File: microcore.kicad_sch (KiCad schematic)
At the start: 5 parts, among them J1 TE_776231-1, J8 USB_B_Mini, M1 Module:mega-mcu100/0.3, M2 Module-power_12and5V-0.3, M3 Module-vr-max9924-0.3

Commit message: Rev p: AOD4184A (C99124) + LS US1M/SMAJ33A + DRC (#9)
* Rev p: AOD4184A on Q1-Q7, LS flyback+TVS, frame short fixes

Quintin chose AOD4184A (LCSC C99124) plus TVS for budget and reliability.
Q5-Q7 get the existing US1M flyback and SMAJ33A. Injector/VR frame shorts
on the board copper are cleared; Hellen module pad-G noise stays documented.

Co-authored-by: Quintin <quintinbannink42@users.noreply.github.com>

* Rev p: keep Q1-Q7 as NCE4080K; LS US1M+SMAJ33A stays

Budget and reliability first. No FET or BOM upgrade and no DPAK land change. Low-side clamps stay the injector US1M and SMAJ33A already in the BOM.

Co-authored-by: Quintin <quintinbannink42@users.noreply.github.com>

---------

Co-authored-by: Quintin <quintinbannink42@users.noreply.github.com>
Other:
- sheet LS3 ports: added V12_RAW; removed none
- note added: "AMPSEAL pins 8/9/10: FP / Idle / Boost (rev p) Q5-Q7 AOD4184A + gate R5-R7 12 ohm + US1M flyback + SMAJ33A"
- note added: "Micro Core rev P MCU mega-mcu100/0.3 STM32F407VGT6 (not mega-mcu64) + power_12and5V/0.3 + vr-max9924/0.3 USB Mini-B + TE 776231-1 AMPSEAL; pins 8/9/10 FP / Idle / Boost Sheets: INJ4 (Q1-Q4) LS3 (Q5-Q7) ANALOG HALL Power FETs AOD4184A C99124. RDS(on) at 4.5 V; Vth max 2.6 V; gate is 3.3 V. coreefi_micro needs F407 target later"
- note removed: "AMPSEAL pins 8/9/10: FP / Idle / Boost (rev o) Q5-Q7 NCE4080K + gate R5-R7 12 ohm"
- note removed: "Micro Core rev O MCU mega-mcu100/0.3 STM32F407VGT6 (not mega-mcu64) + power_12and5V/0.3 + vr-max9924/0.3 USB Mini-B + TE 776231-1 AMPSEAL; pins 8/9/10 FP / Idle / Boost Sheets: INJ4 (Q1-Q4) LS3 (Q5-Q7) ANALOG HALL Power FETs NCE4080K C191380. coreefi_micro needs F407 target later"
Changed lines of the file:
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@@
 	(title_block
 		(title "Micro Core")
-		(date "2026-09-22")
-		(rev "O")
+		(date "2026-09-24")
+		(rev "P")
 		(company "Core EFI")
-		(comment 1 "rev o: NCE4080K Q1-Q7; LS Q5-Q7 restored; F407VGT6 stays")
+		(comment 1 "rev p: AOD4184A Q1-Q7 C99124; LS flyback+TVS; F407VGT6 stays")
 		(comment 2 "Firmware board: coreefi_micro — needs F407 target later; fw not in this repo")
 		(comment 3 "PCB basename: microcore (no dashes/underscores)")
@@
 			)
 		)
+		(pin "V12_RAW" input
+			(at 17.78 70.14 90)
+			(effects
+				(font
+					(size 1.27 1.27)
+				)
+				(justify left)
+			)
+		)
 		(instances
 			(project "microcore"
@@
 		)
 	)
-	(text "Micro Core rev O\nMCU mega-mcu100/0.3 STM32F407VGT6 (not mega-mcu64) + power_12and5V/0.3 + vr-max9924/0.3\nUSB Mini-B + TE 776231-1 AMPSEAL; pins 8/9/10 FP / Idle / Boost\nSheets: INJ4 (Q1-Q4) LS3 (Q5-Q7) ANALOG HALL\nPower FETs NCE4080K C191380. coreefi_micro needs F407 target later"
+	(text "Micro Core rev P\nMCU mega-mcu100/0.3 STM32F407VGT6 (not mega-mcu64) + power_12and5V/0.3 + vr-max9924/0.3\nUSB Mini-B + TE 776231-1 AMPSEAL; pins 8/9/10 FP / Idle / Boost\nSheets: INJ4 (Q1-Q4) LS3 (Q5-Q7) ANALOG HALL\nPower FETs AOD4184A C99124. RDS(on) at 4.5 V; Vth max 2.6 V; gate is 3.3 V. coreefi_micro needs F407 target later"
 		(exclude_from_sim no)
 		(at 25.4 280 0)
@@
 		)
 	)
-	(text "AMPSEAL pins 8/9/10: FP / Idle / Boost (rev o)\nQ5-Q7 NCE4080K + gate R5-R7 12 ohm"
+	(text "AMPSEAL pins 8/9/10: FP / Idle / Boost (rev p)\nQ5-Q7 AOD4184A + gate R5-R7 12 ohm + US1M flyback + SMAJ33A"
 		(exclude_from_sim no)
 		(at 230 43.18 0)
 		(effects
 			(font
+				(size 1.27 1.27)
+			)
+			(justify left bottom)
+		)
+	)
+	(wire
+		(pts
+			(xy 17.78 70.14) (xy 17.78 67.31)
+		)
+		(stroke
+			(width 0)
+			(type default)
+		)
+	)
+	(label "V12_RAW"
+		(at 17.78 67.31 90)
+		(effects
+			(font

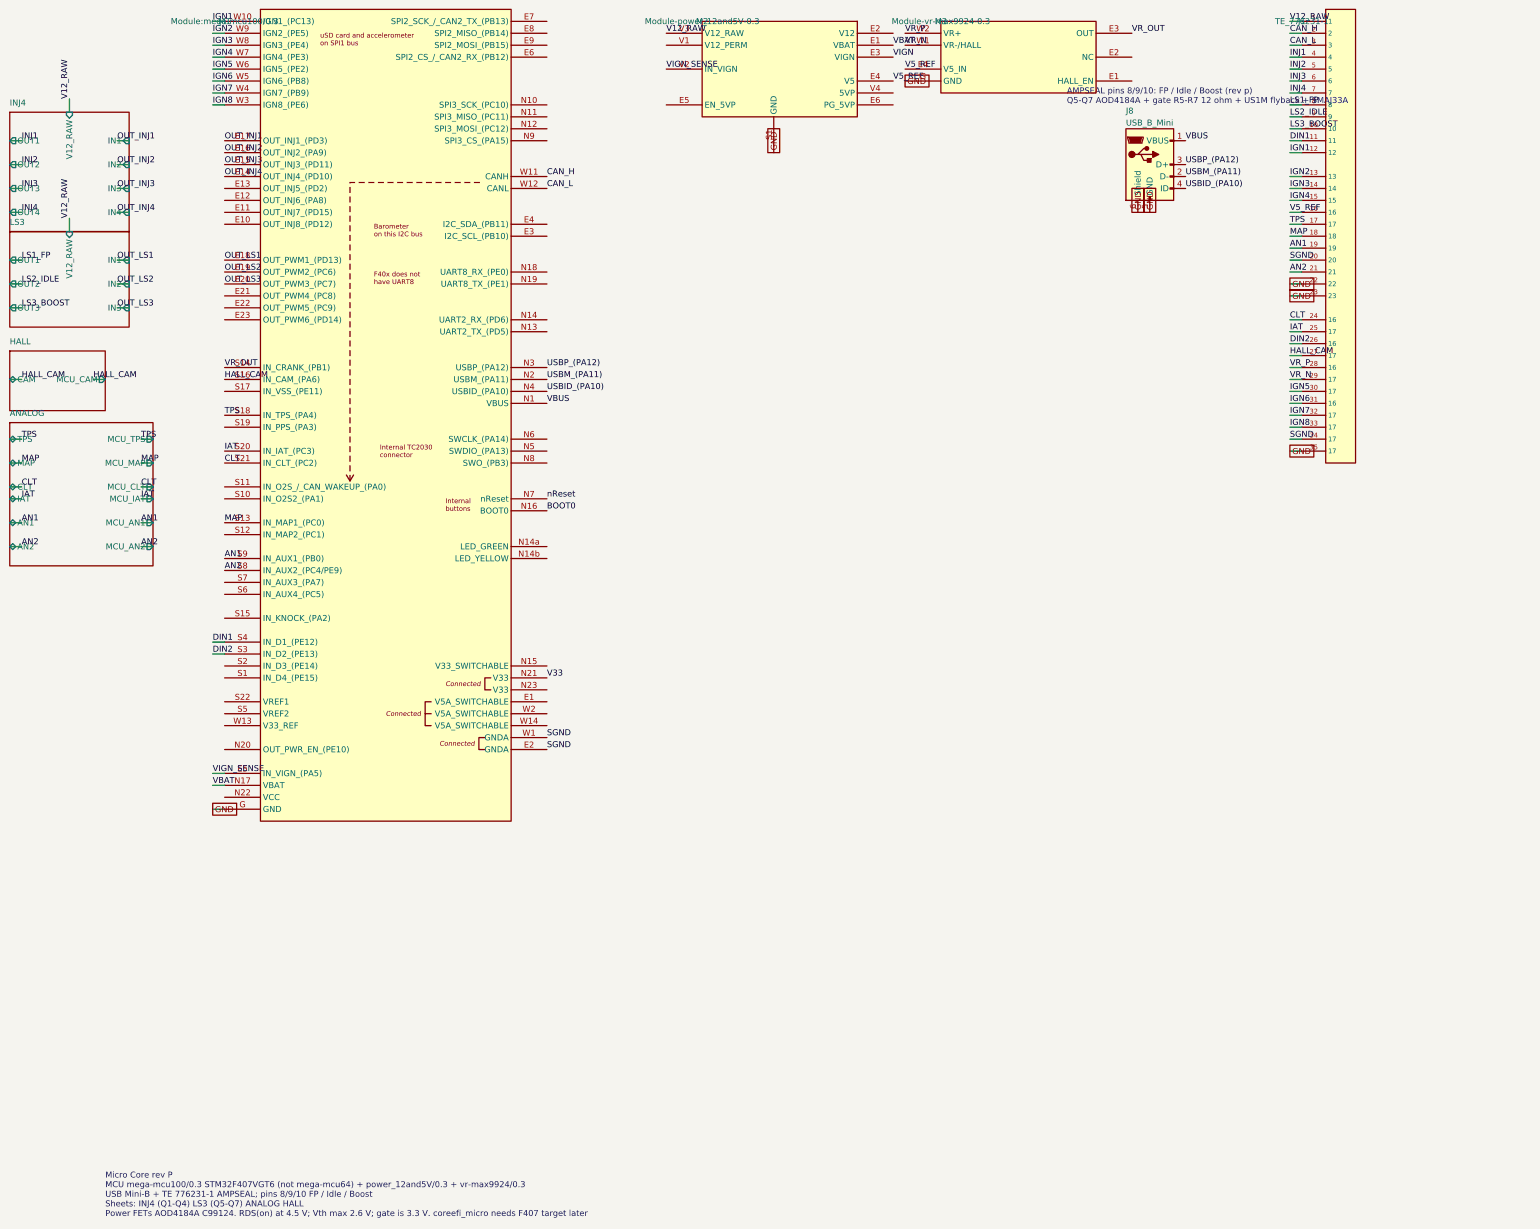
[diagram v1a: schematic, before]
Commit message: Rev q: NCE4080K (C191380) plus SLM27524 gate drivers on V12_RAW
Restore Q1-Q7 to NCE4080K and insert four SLM27524CA-DG drivers so the
STM32 GPIO no longer drives the FET gates. Seven channels are used; the
spare input is tied to GND. LS clamps and the rev p short fixes stay.

Co-authored-by: Quintin <quintinbannink42@users.noreply.github.com>
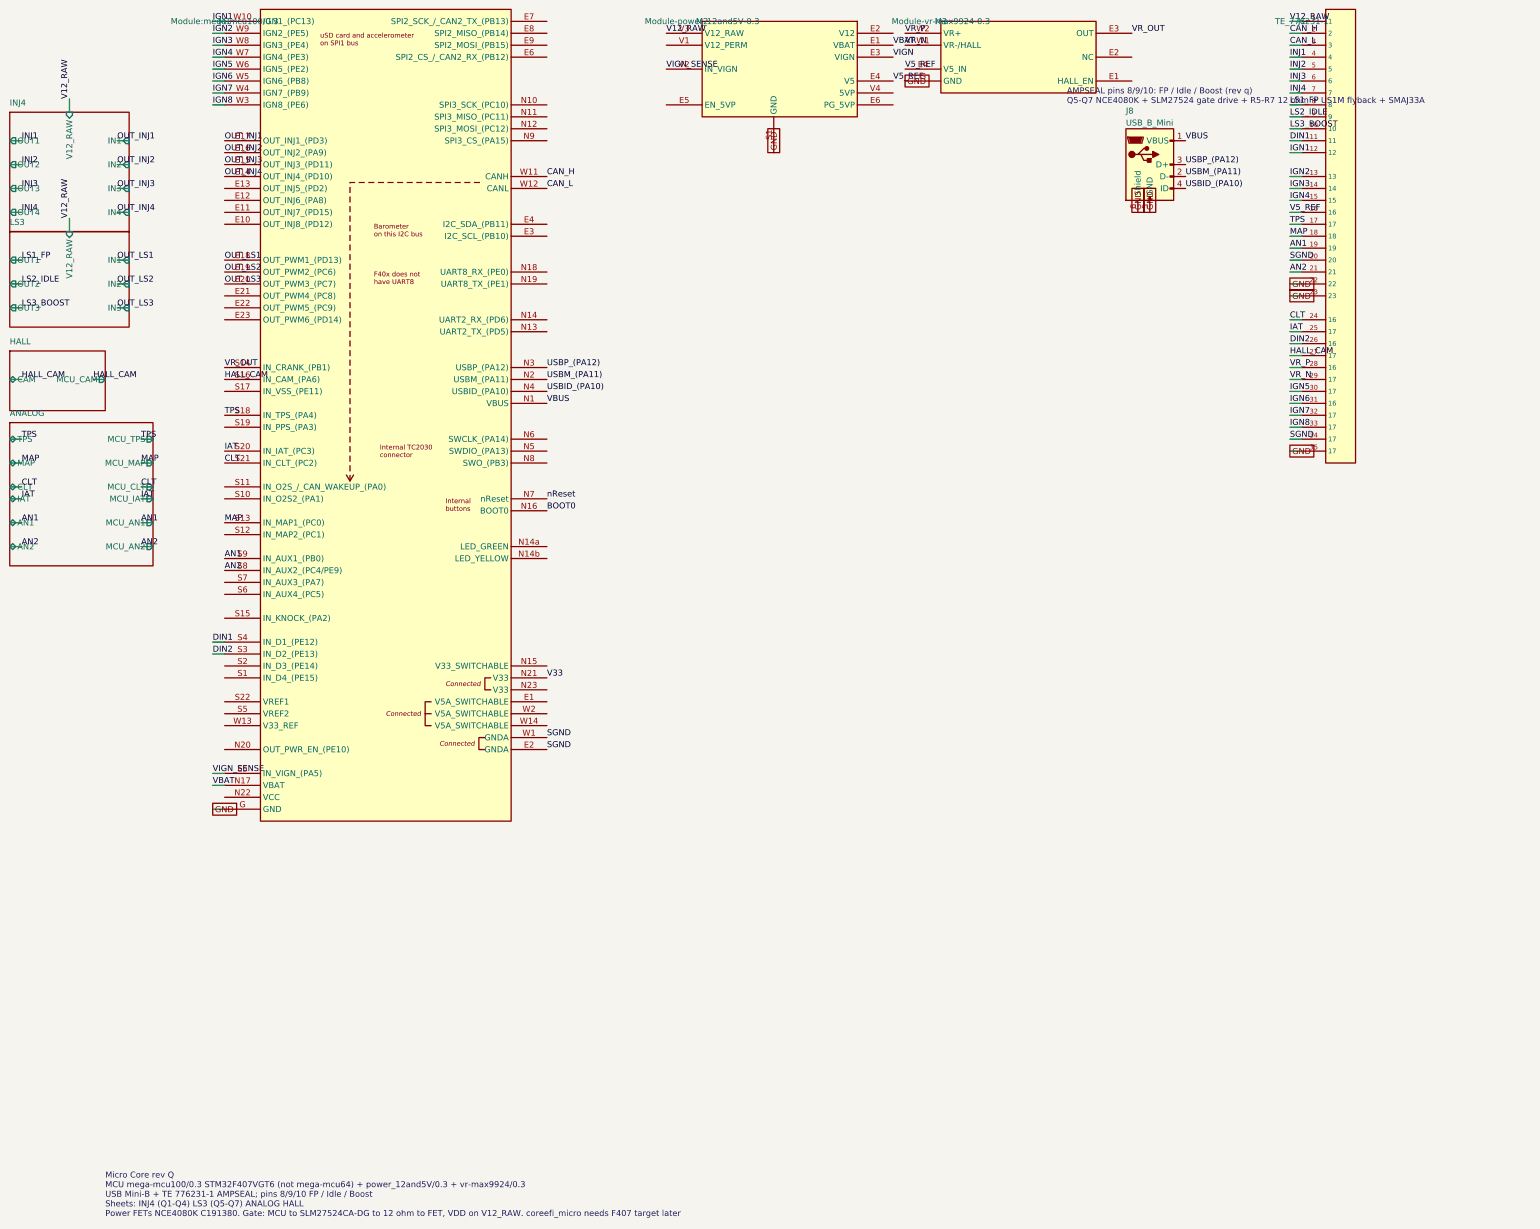
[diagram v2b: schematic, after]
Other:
- note added: "AMPSEAL pins 8/9/10: FP / Idle / Boost (rev q) Q5-Q7 NCE4080K + SLM27524 gate drive + R5-R7 12 ohm + US1M flyback + SMAJ33A"
- note added: "Micro Core rev Q MCU mega-mcu100/0.3 STM32F407VGT6 (not mega-mcu64) + power_12and5V/0.3 + vr-max9924/0.3 USB Mini-B + TE 776231-1 AMPSEAL; pins 8/9/10 FP / Idle / Boost Sheets: INJ4 (Q1-Q4) LS3 (Q5-Q7) ANALOG HALL Power FETs NCE4080K C191380. Gate: MCU to SLM27524CA-DG to 12 ohm to FET, VDD on V12_RAW. coreefi_micro needs F407 target later"
- note removed: "AMPSEAL pins 8/9/10: FP / Idle / Boost (rev p) Q5-Q7 AOD4184A + gate R5-R7 12 ohm + US1M flyback + SMAJ33A"
- note removed: "Micro Core rev P MCU mega-mcu100/0.3 STM32F407VGT6 (not mega-mcu64) + power_12and5V/0.3 + vr-max9924/0.3 USB Mini-B + TE 776231-1 AMPSEAL; pins 8/9/10 FP / Idle / Boost Sheets: INJ4 (Q1-Q4) LS3 (Q5-Q7) ANALOG HALL Power FETs AOD4184A C99124. RDS(on) at 4.5 V; Vth max 2.6 V; gate is 3.3 V. coreefi_micro needs F407 target later"
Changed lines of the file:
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@@
 	(title_block
 		(title "Micro Core")
-		(date "2026-09-24")
-		(rev "P")
+		(date "2026-09-26")
+		(rev "Q")
 		(company "Core EFI")
-		(comment 1 "rev p: AOD4184A Q1-Q7 C99124; LS flyback+TVS; F407VGT6 stays")
+		(comment 1 "rev q: NCE4080K Q1-Q7 C191380; SLM27524 gate drivers; LS clamps kept")
 		(comment 2 "Firmware board: coreefi_micro — needs F407 target later; fw not in this repo")
 		(comment 3 "PCB basename: microcore (no dashes/underscores)")
@@
 		)
 	)
-	(text "Micro Core rev P\nMCU mega-mcu100/0.3 STM32F407VGT6 (not mega-mcu64) + power_12and5V/0.3 + vr-max9924/0.3\nUSB Mini-B + TE 776231-1 AMPSEAL; pins 8/9/10 FP / Idle / Boost\nSheets: INJ4 (Q1-Q4) LS3 (Q5-Q7) ANALOG HALL\nPower FETs AOD4184A C99124. RDS(on) at 4.5 V; Vth max 2.6 V; gate is 3.3 V. coreefi_micro needs F407 target later"
+	(text "Micro Core rev Q\nMCU mega-mcu100/0.3 STM32F407VGT6 (not mega-mcu64) + power_12and5V/0.3 + vr-max9924/0.3\nUSB Mini-B + TE 776231-1 AMPSEAL; pins 8/9/10 FP / Idle / Boost\nSheets: INJ4 (Q1-Q4) LS3 (Q5-Q7) ANALOG HALL\nPower FETs NCE4080K C191380. Gate: MCU to SLM27524CA-DG to 12 ohm to FET, VDD on V12_RAW. coreefi_micro needs F407 target later"
 		(exclude_from_sim no)
 		(at 25.4 280 0)
@@
 		)
 	)
-	(text "AMPSEAL pins 8/9/10: FP / Idle / Boost (rev p)\nQ5-Q7 AOD4184A + gate R5-R7 12 ohm + US1M flyback + SMAJ33A"
+	(text "AMPSEAL pins 8/9/10: FP / Idle / Boost (rev q)\nQ5-Q7 NCE4080K + SLM27524 gate drive + R5-R7 12 ohm + US1M flyback + SMAJ33A"
 		(exclude_from_sim no)
 		(at 230 43.18 0)
